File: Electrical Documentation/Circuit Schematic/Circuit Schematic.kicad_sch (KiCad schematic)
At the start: 26 parts, among them J1 Conn_01x03, J10 Conn_01x04, J11 Conn_01x04, J12 Conn_01x04, J13 Conn_01x04, J14 Conn_01x04, J15 Conn_01x04, J2 Conn_01x03, J3 Conn_01x03, J4 Conn_01x03, J5 Conn_01x03, J6 Conn_01x03, J7 Conn_01x03, J8 Conn_01x03, J9 Conn_01x03, Q1 NMOS, Q2 NPN

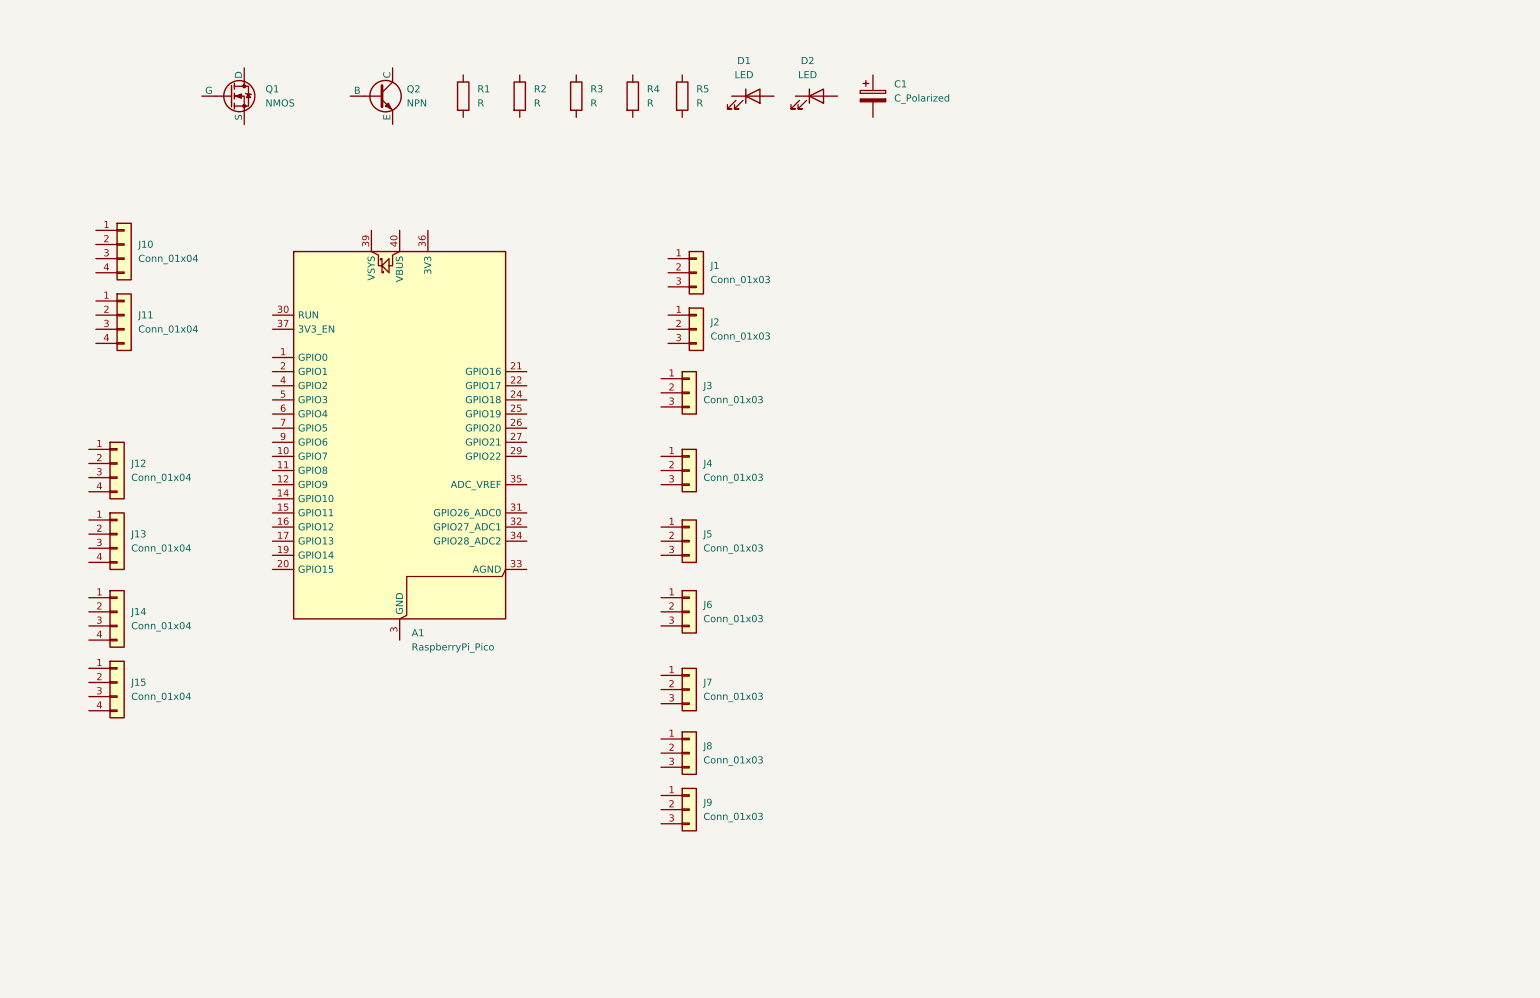
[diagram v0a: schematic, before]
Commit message: Started Circuit Documentation
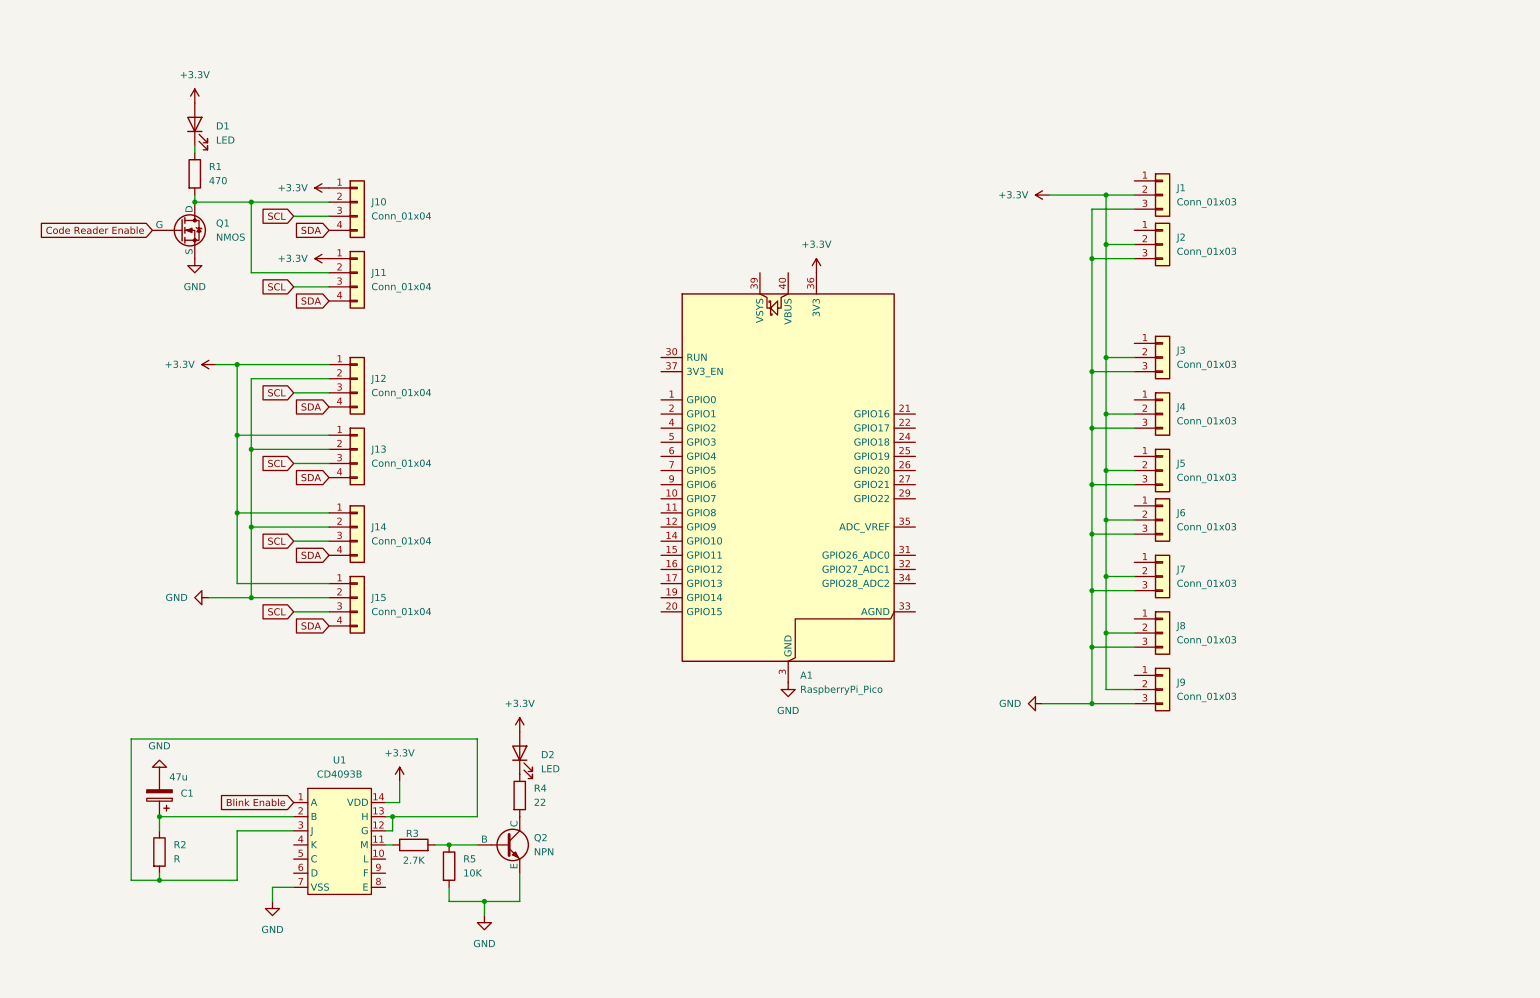
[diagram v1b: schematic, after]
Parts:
- added U1: CD4093B, symbol Component_Symbols:CD4093B
- C1: value C_Polarized -> 47u
- R1: value R -> 470
- R3: value R -> 2.7K
- R4: value R -> 22
- R5: value R -> 10K
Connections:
- net +3.3V: now reaches J12.1 (Pin_1)
- net +3.3V: now also A1.36 (3V3), D1.2 (A), D2.2 (A), J1.2 (Pin_2), J10.1 (Pin_1), J11.1 (Pin_1), J13.1 (Pin_1), J14.1 (Pin_1), J15.1 (Pin_1), J2.2 (Pin_2), J3.2 (Pin_2), J4.2 (Pin_2), J5.2 (Pin_2), J6.2 (Pin_2), J7.2 (Pin_2), J8.2 (Pin_2), J9.2 (Pin_2), U1.14 (VDD)
- net GND: now reaches J12.2 (Pin_2)
- net GND: now also A1.13 (GND), A1.18 (GND), A1.23 (GND), A1.28 (GND), A1.3 (GND), A1.38 (GND), A1.8 (GND), C1.2, J1.3 (Pin_3), J13.2 (Pin_2), J14.2 (Pin_2), J15.2 (Pin_2), J2.3 (Pin_3), J3.3 (Pin_3), J4.3 (Pin_3), J5.3 (Pin_3), J6.3 (Pin_3), J7.3 (Pin_3), J8.3 (Pin_3), J9.3 (Pin_3), Q1.3 (S), Q2.3 (E), R5.2, U1.7 (VSS)
- net SCL: now reaches J12.3 (Pin_3)
- net SCL: now also J10.3 (Pin_3), J11.3 (Pin_3), J13.3 (Pin_3), J14.3 (Pin_3), J15.3 (Pin_3)
- net SDA: now reaches J12.4 (Pin_4)
- net SDA: now also J10.4 (Pin_4), J11.4 (Pin_4), J13.4 (Pin_4), J14.4 (Pin_4), J15.4 (Pin_4)
- net at R3.1: now also U1.11 (M)
- net at R3.2: now also Q2.2 (B), R5.1
- net at Q1.1 (D): now also J10.2 (Pin_2), J11.2 (Pin_2), R1.2
- net Code Reader Enable: now reaches Q1.2 (G)
- net at D1.1 (K): now also R1.1
- net at R2.1: now also C1.1, U1.2 (B)
- net at R2.2: now also U1.12 (G), U1.13 (H), U1.3 (J)
- net at R4.1: now also D2.1 (K)
- net at R4.2: now also Q2.1 (C)
- new net Blink Enable: U1.1 (A)
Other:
- moved on the sheet: A1, C1, D1, D2, J1, J10, J11, J12, J13, J14, J15, J2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

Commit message: Finished 1st draft of circuit documentation
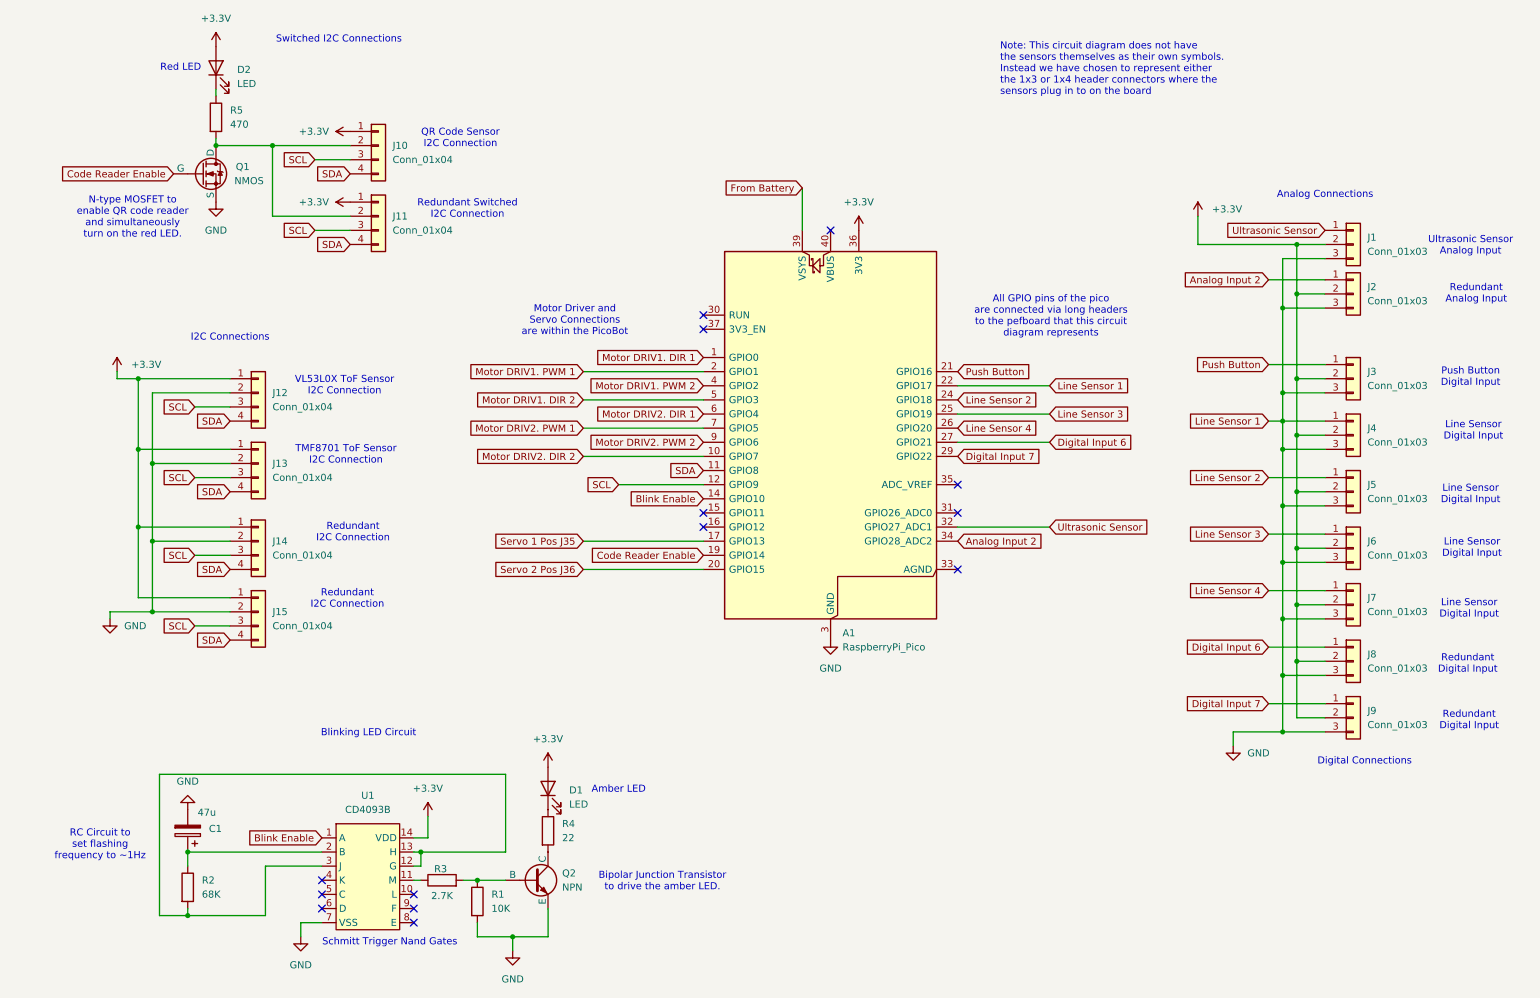
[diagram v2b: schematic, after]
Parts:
- R2: value R -> 68K
- renumbered D2 to D1, D1 to D2, R5 to R1, R1 to R5
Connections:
- net Blink Enable: now also A1.14 (GPIO10)
- net Code Reader Enable: now also A1.19 (GPIO14)
- net GND: now also A1.22 (GPIO17), J4.1 (Pin_1)
- net SCL: now also A1.12 (GPIO9)
- net SDA: now also A1.11 (GPIO8)
- net Line Sensor 3: now reaches J6.1 (Pin_1)
- net Line Sensor 3: now also A1.25 (GPIO19)
- net Motor DRIV1. DIR 1: now reaches A1.1 (GPIO0)
- net Motor DRIV2. DIR 2: now reaches A1.10 (GPIO7)
- net Servo 1 Pos J35: now reaches A1.17 (GPIO13)
- net Motor DRIV1. PWM 1: now reaches A1.2 (GPIO1)
- net Servo 2 Pos J36: now reaches A1.20 (GPIO15)
- net Push Button: now reaches A1.21 (GPIO16)
- net Push Button: now also J3.1 (Pin_1)
- net Line Sensor 2: now reaches A1.24 (GPIO18)
- net Line Sensor 2: now also J5.1 (Pin_1)
- net Line Sensor 4: now reaches A1.26 (GPIO20)
- net Line Sensor 4: now also J7.1 (Pin_1)
- net Digital Input 6: now reaches A1.27 (GPIO21)
- net Digital Input 6: now also J8.1 (Pin_1)
- net Digital Input 7: now reaches A1.29 (GPIO22)
- net Digital Input 7: now also J9.1 (Pin_1)
- net Ultrasonic Sensor: now reaches A1.32 (GPIO27_ADC1)
- net Ultrasonic Sensor: now also J1.1 (Pin_1)
- net Analog Input 2: now reaches A1.34 (GPIO28_ADC2)
- net Analog Input 2: now also J2.1 (Pin_1)
- net From Battery: now reaches A1.39 (VSYS)
- net Motor DRIV1. PWM 2: now reaches A1.4 (GPIO2)
- net Motor DRIV1. DIR 2: now reaches A1.5 (GPIO3)
- net Motor DRIV2. DIR 1: now reaches A1.6 (GPIO4)
- net Motor DRIV2. PWM 1: now reaches A1.7 (GPIO5)
- net Motor DRIV2. PWM 2: now reaches A1.9 (GPIO6)
- no-connect marks 0 -> 14
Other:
- note added: "All GPIO pins of the pico are connected via long headers to the pefboard that this circuit diagram represents"
- note added: "Amber LED"
- note added: "Analog Connections"
- note added: "Bipolar Junction Transistor to drive the amber LED."
- note added: "Blinking LED Circuit"
- note added: "Digital Connections"
- note added: "I2C Connections"
- note added: "Line Sensor Digital Input"
- note added: "Motor Driver and Servo Connections are within the PicoBot"
- note added: "N-type MOSFET to enable QR code reader and simultaneously turn on the red LED."
- note added: "Note: This circuit diagram does not have the sensors themselves as their own symbols. Instead we have chosen to represent either the 1x3 or 1x4 header connectors where the sensors plug in to on the board"
- note added: "Push Button Digital Input"
- note added: "QR Code Sensor I2C Connection"
- note added: "RC Circuit to set flashing frequency to ~1Hz"
- note added: "Red LED"
- note added: "Redundant Analog Input"
- note added: "Redundant Digital Input"
- note added: "Redundant I2C Connection"
- note added: "Redundant Switched I2C Connection"
- note added: "Schmitt Trigger Nand Gates"
- note added: "Switched I2C Connections"
- note added: "TMF8701 ToF Sensor I2C Connection"
- note added: "Ultrasonic Sensor Analog Input"
- note added: "VL53L0X ToF Sensor I2C Connection"
- title: (none) -> IDP Team M103 Circuit Drawings
- moved on the sheet: A1, C1, D1, D2, J1, J10, J11, J12, J13, J14, J15, J2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

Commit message: Final draft of circuit documentation
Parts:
- renumbered U1 to IC1
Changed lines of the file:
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@@
 		(dnp no)
 		(fields_autoplaced yes)
-		(property "Reference" "U1"
+		(property "Reference" "IC1"
 			(at 75.565 160.02 0)
 			(effects
@@
 			(project ""
 				(path "/c2e13abb-d55e-494f-892f-f4034ec589d2"
-					(reference "U1")
+					(reference "IC1")
 					(unit 1)
 				)

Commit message: Electrical Documentation updates
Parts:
- removed J8, J9: Conn_01x03, symbol Connector_Generic:Conn_01x03
- Q1: renamed from Q2; value NPN -> 2N3904
- Q2: renamed from Q1; value NMOS -> ZVN4306A
- R4: value 22 -> 390
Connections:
- net Digital Input 6 is gone; now on net Line Sensor 3: A1.27 (GPIO21)
- net Digital Input 7 is gone; now on net Line Sensor 4: A1.29 (GPIO22)
- net GND: no longer A1.22 (GPIO17), J4.1 (Pin_1)
- net Line Sensor 2: now also A1.26 (GPIO20); no longer A1.24 (GPIO18)
- net Line Sensor 3: no longer A1.25 (GPIO19)
- net Line Sensor 4: no longer A1.26 (GPIO20)
- net From Battery renamed Battery
- net SCL renamed SCL 0
- net SCL 0: no longer J10.3 (Pin_3), J11.3 (Pin_3)
- net SDA renamed SDA 0
- net SDA 0: no longer J10.4 (Pin_4), J11.4 (Pin_4)
- new net Line Sensor 1: A1.22 (GPIO17), J4.1 (Pin_1)
- new net SCL 1: A1.25 (GPIO19), J10.3 (Pin_3), J11.3 (Pin_3)
- new net SDA 1: A1.24 (GPIO18), J10.4 (Pin_4), J11.4 (Pin_4)
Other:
- note added: "All GPIO pins of the pico are connected via long headers to the pefboard that this circuit diagram represents."
- note added: "I2C Connections on Bus 0"
- note added: "Motor driver and servo connections are within the PicoBot."
- note added: "RC circuit to set flashing frequency to ~1Hz."
- note added: "Switched I2C Connections on Bus 1"
- note removed: "All GPIO pins of the pico are connected via long headers to the pefboard that this circuit diagram represents"
- note removed: "I2C Connections"
- note removed: "Motor Driver and Servo Connections are within the PicoBot"
- note removed: "RC Circuit to set flashing frequency to ~1Hz"
- note removed: "Redundant Digital Input"
- note removed: "Switched I2C Connections"
- moved on the sheet: D2, J10, J11, Q2, R5

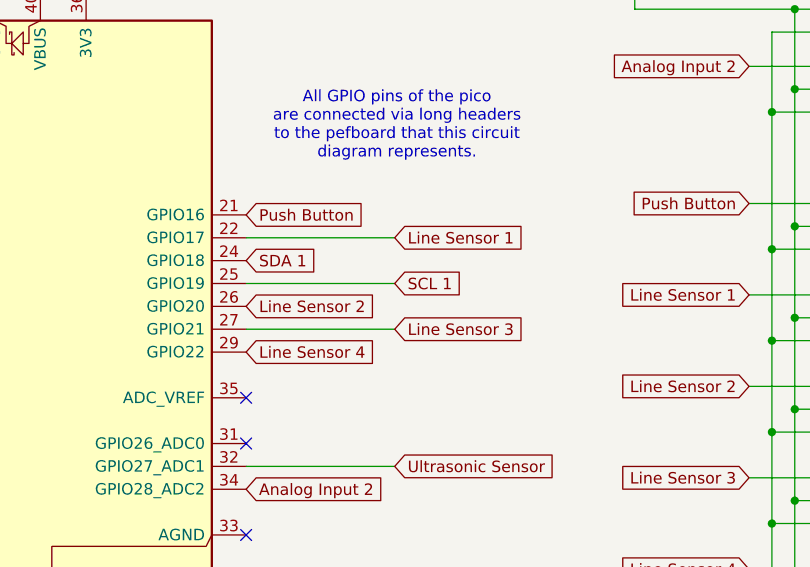
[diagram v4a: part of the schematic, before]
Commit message: Schematic Updates
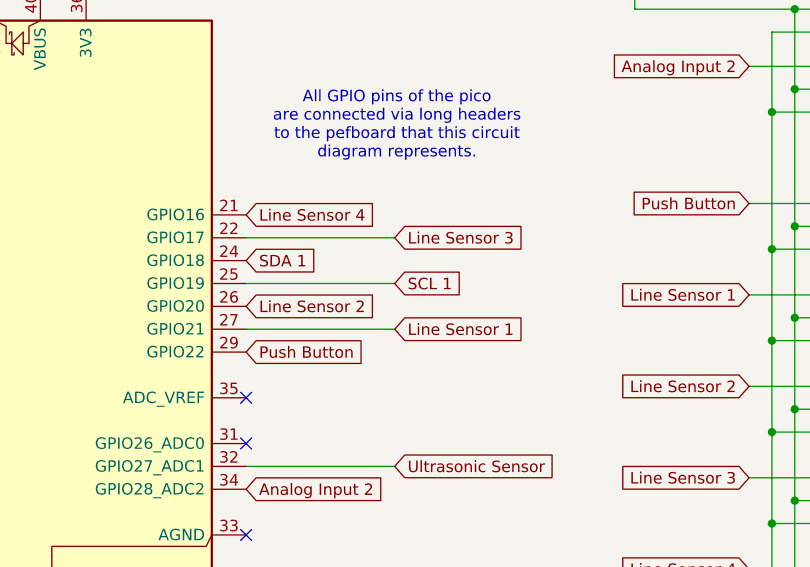
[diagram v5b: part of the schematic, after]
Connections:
- net Line Sensor 1: now also A1.27 (GPIO21); no longer A1.22 (GPIO17)
- net Line Sensor 3: now also A1.22 (GPIO17); no longer A1.27 (GPIO21)
- net Line Sensor 4: now also A1.21 (GPIO16); no longer A1.29 (GPIO22)
- net Push Button: now also A1.29 (GPIO22); no longer A1.21 (GPIO16)
